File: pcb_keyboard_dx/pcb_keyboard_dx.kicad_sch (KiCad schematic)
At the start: 131 parts, among them SW1 BOOT button, U1 Pico, U2 74LVC1G34, U3 TRRS

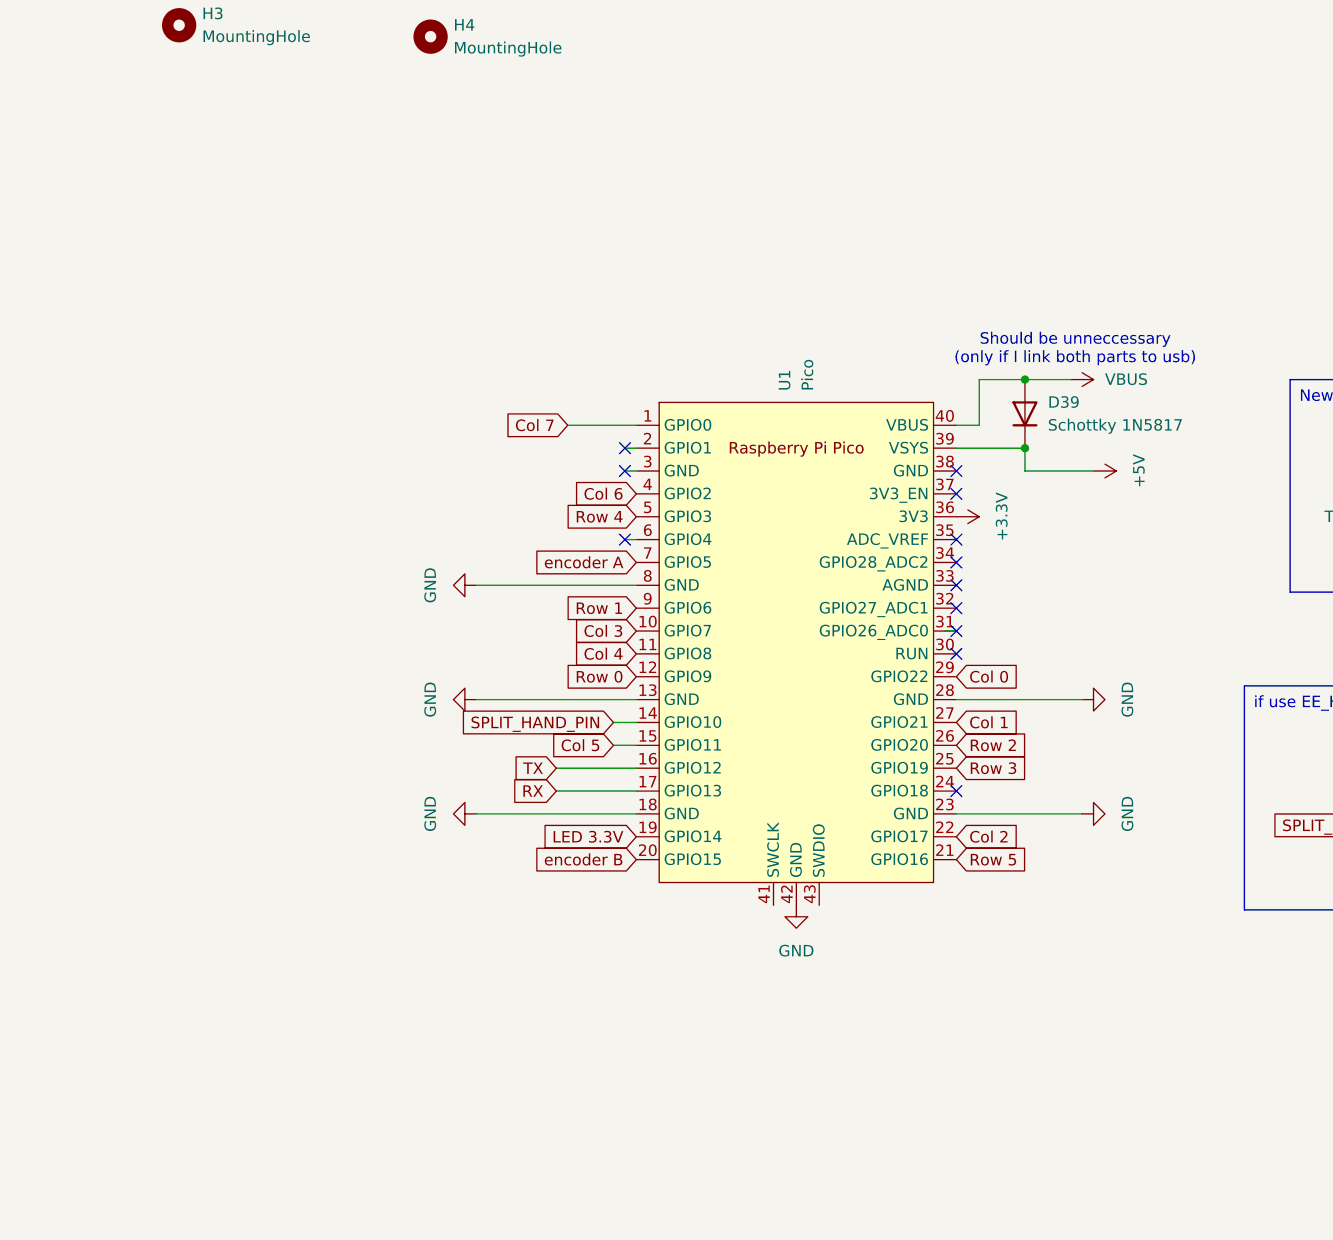
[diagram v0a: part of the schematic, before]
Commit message: added d+ and d- bus
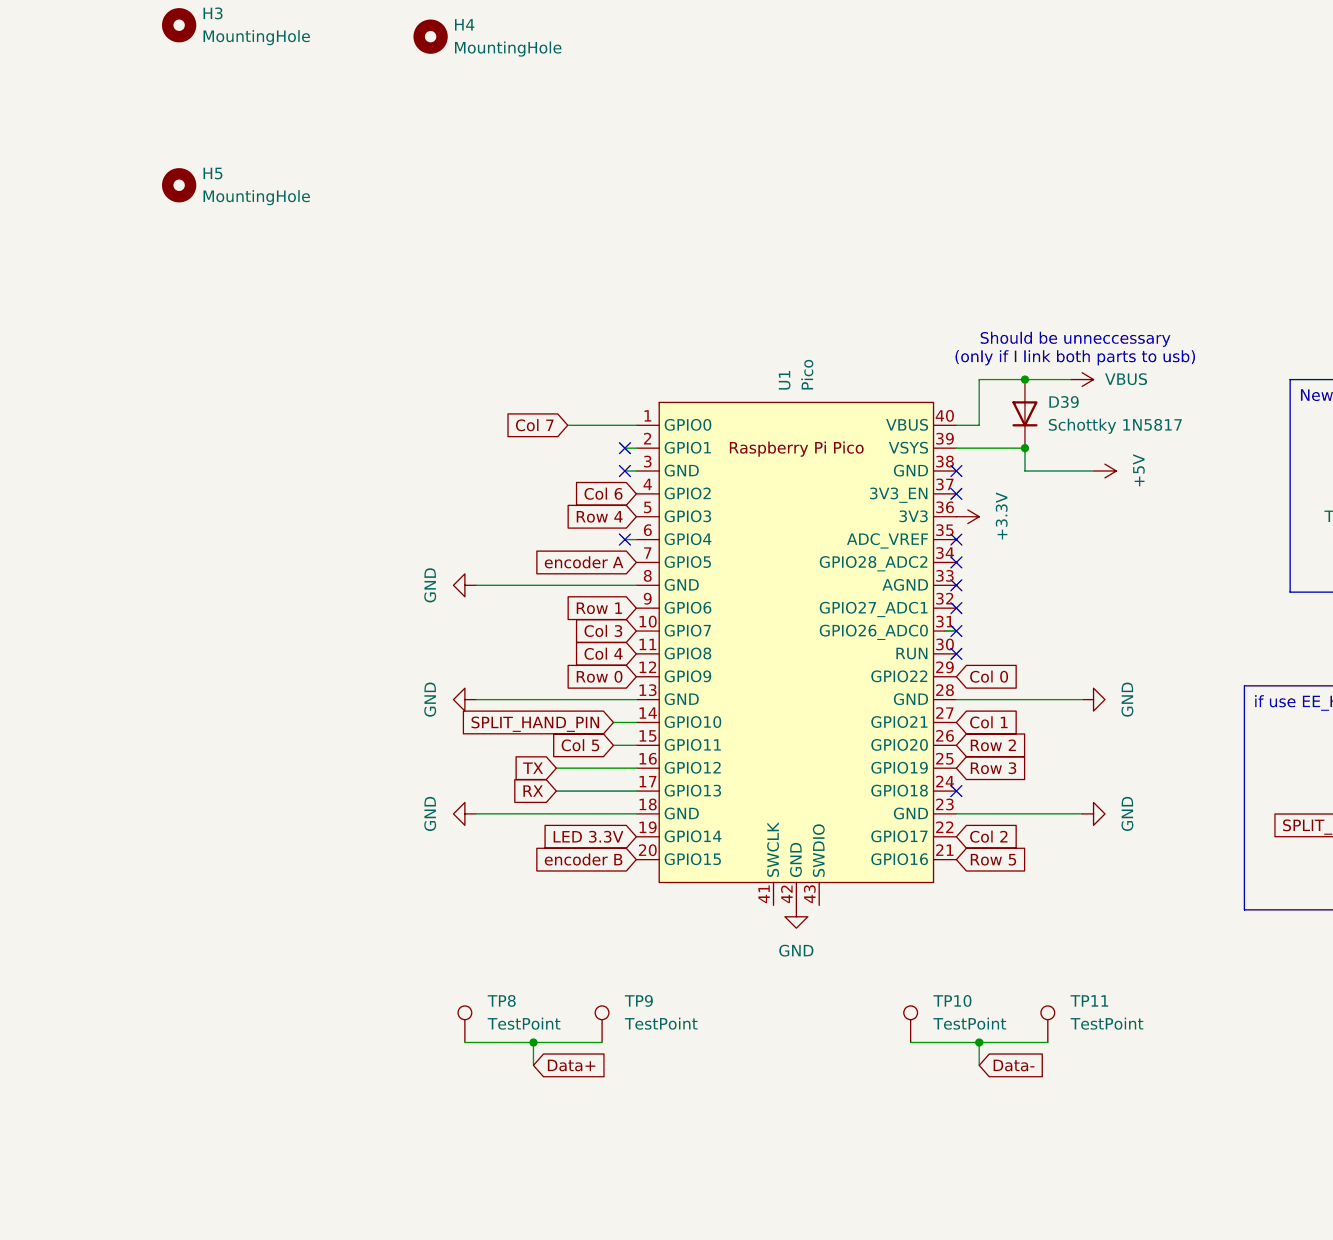
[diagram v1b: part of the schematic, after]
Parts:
- added H5: MountingHole, MountingHole:MountingHole_3.2mm_M3, symbol Mechanical:MountingHole
- added TP10, TP11, TP8, TP9: TestPoint, Connector_PinHeader_2.54mm:PinHeader_1x01_P2.54mm_Vertical, symbol Connector:TestPoint
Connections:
- new net Data+: TP8.1, TP9.1
- new net Data-: TP10.1, TP11.1

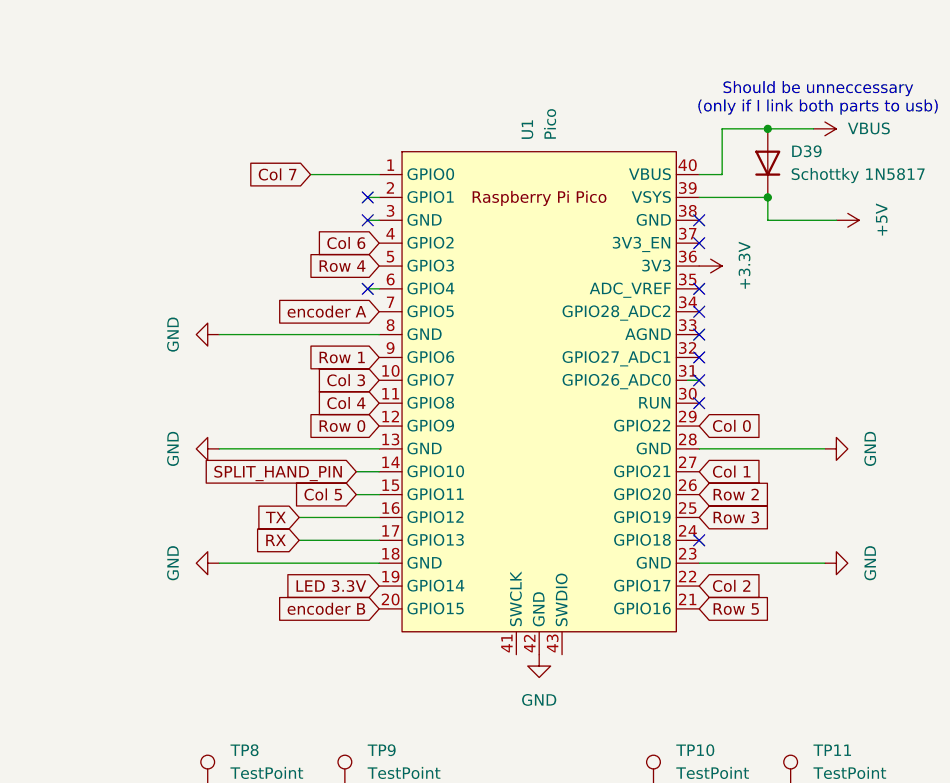
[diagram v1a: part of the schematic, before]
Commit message: stessi GPIO per dx e sx
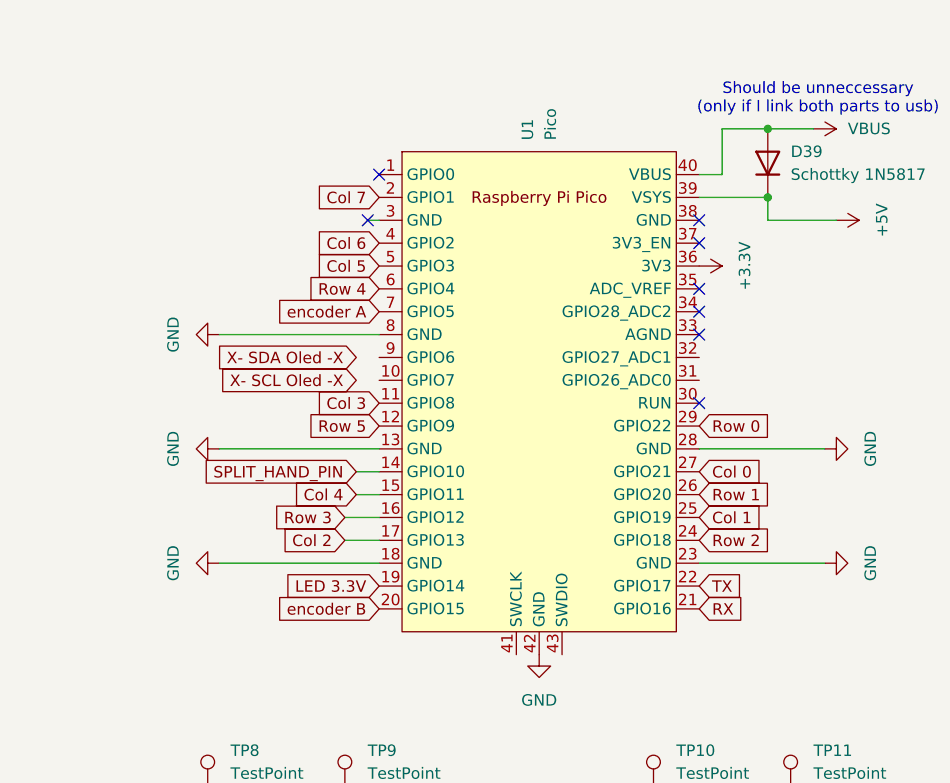
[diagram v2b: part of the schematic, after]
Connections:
- net Col 0: now also U1.27 (GPIO21); no longer U1.29 (GPIO22)
- net Col 1: now also U1.25 (GPIO19); no longer U1.27 (GPIO21)
- net Col 2: now also U1.17 (GPIO13); no longer U1.22 (GPIO17)
- net Col 3: now also U1.11 (GPIO8); no longer U1.10 (GPIO7)
- net Col 4: now also U1.15 (GPIO11); no longer U1.11 (GPIO8)
- net Col 5: now also U1.5 (GPIO3); no longer U1.15 (GPIO11)
- net Col 7: now also U1.2 (GPIO1); no longer U1.1 (GPIO0)
- net RX: now also U1.21 (GPIO16); no longer U1.17 (GPIO13)
- net Row 0: now also U1.29 (GPIO22); no longer U1.12 (GPIO9)
- net Row 1: now also U1.26 (GPIO20); no longer U1.9 (GPIO6)
- net Row 2: now also U1.24 (GPIO18); no longer U1.26 (GPIO20)
- net Row 3: now also U1.16 (GPIO12); no longer U1.25 (GPIO19)
- net Row 4: now also U1.6 (GPIO4); no longer U1.5 (GPIO3)
- net Row 5: now also U1.12 (GPIO9); no longer U1.21 (GPIO16)
- net TX: now also U1.22 (GPIO17); no longer U1.16 (GPIO12)
- no-connect marks 12 -> 8
